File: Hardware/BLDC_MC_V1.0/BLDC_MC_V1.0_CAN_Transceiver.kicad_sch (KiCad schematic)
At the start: 15 parts, among them U2 TCAN334DR

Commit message: Update recovery files of the project
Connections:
- net IC_TXD: now reaches R11.1, U2.1 (TXD)
- net IC_RXD: now reaches R12.1, U2.4 (RXD)
- net SHDN: now reaches C15.1, R9.1, U2.5 (SHDN)
- net CANL: now reaches FL1.2, U2.6 (CANL)
- net CANH: now reaches FL1.1, U2.7 (CANH)
- net STB: now reaches C14.1, R10.1, U2.8 (STB)
- net Split_CAP: now reaches C16.1, R13.2, R14.1
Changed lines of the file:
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@@
+		)
+	)
+	(label "SHDN"
+		(at 110.49 83.82 0)
+		(effects
+			(font
+				(size 1.27 1.27)
+			)
+			(justify left bottom)
+		)
+	)
+	(label "CANH"
+		(at 157.48 83.82 0)
+		(effects
+			(font
+				(size 1.27 1.27)
+			)
+			(justify left bottom)
+		)
+	)
+	(label "IC_RXD"
+		(at 107.95 91.44 0)
+		(effects
+			(font
+				(size 1.27 1.27)
+			)
+			(justify left bottom)
+		)
+	)
+	(label "STB"
+		(at 110.49 86.36 0)
+		(effects
+			(font
+				(size 1.27 1.27)
+			)
+			(justify left bottom)
+		)
+	)
+	(label "CANL"
+		(at 157.48 91.44 0)
+		(effects
+			(font
+				(size 1.27 1.27)
+			)
+			(justify left bottom)
+		)
+	)
+	(label "IC_TXD"
+		(at 107.95 88.9 0)
+		(effects
+			(font
+				(size 1.27 1.27)
+			)
+			(justify left bottom)
+		)
+	)
+	(label "Split_CAP"
+		(at 203.2 87.63 0)
+		(effects
+			(font
+				(size 1.27 1.27)
+			)
+			(justify left bottom)
 		)
 	)

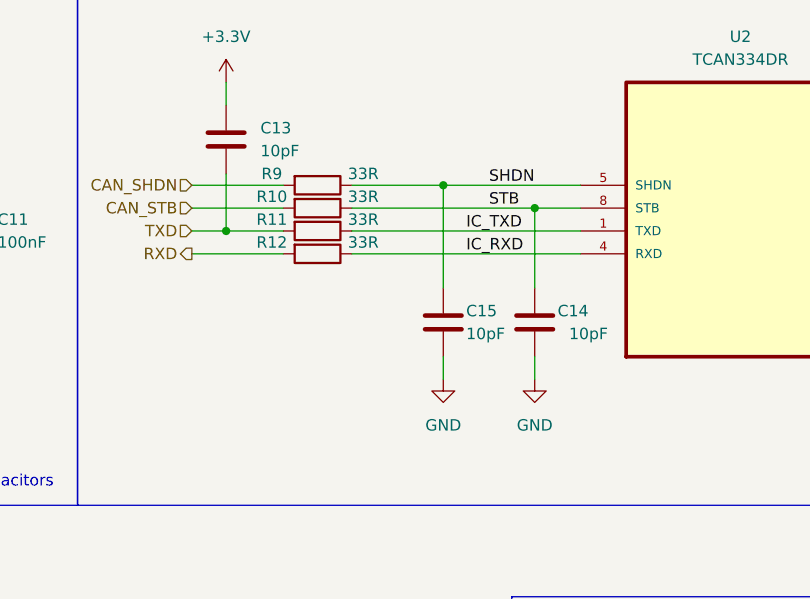
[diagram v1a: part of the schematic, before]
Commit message: Update the component placement of the board
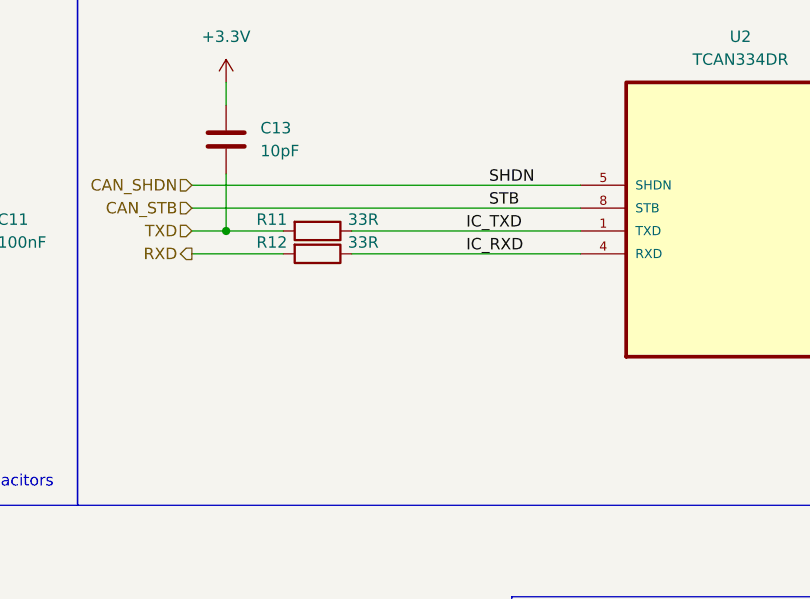
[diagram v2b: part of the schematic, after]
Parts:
- removed C14, C15: 10pF, Capacitor_SMD:C_0603_1608Metric, symbol Device:C
- removed R10, R9: 33R, Resistor_SMD:R_0603_1608Metric, symbol Device:R
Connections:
- net SHDN is gone; now on net CAN_SHDN: U2.5 (SHDN)
- net STB is gone; now on net CAN_STB: U2.8 (STB)

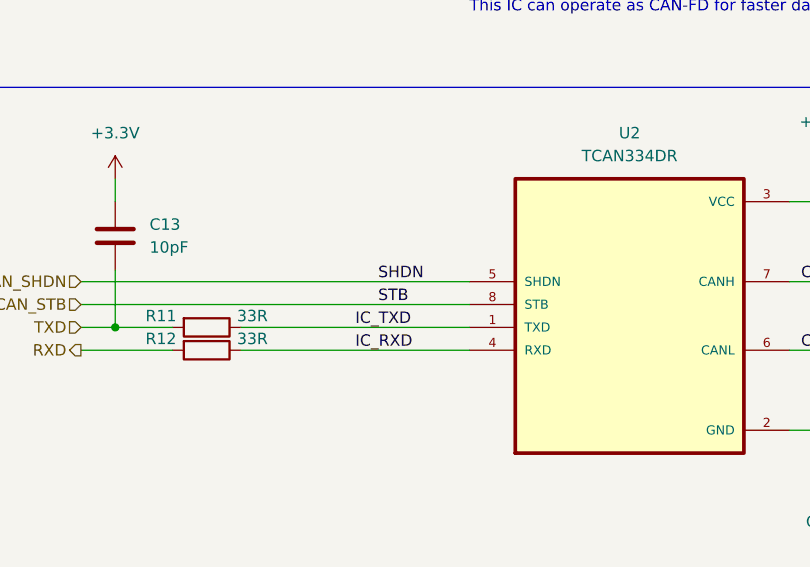
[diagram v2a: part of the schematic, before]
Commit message: Update the components' placement of the board
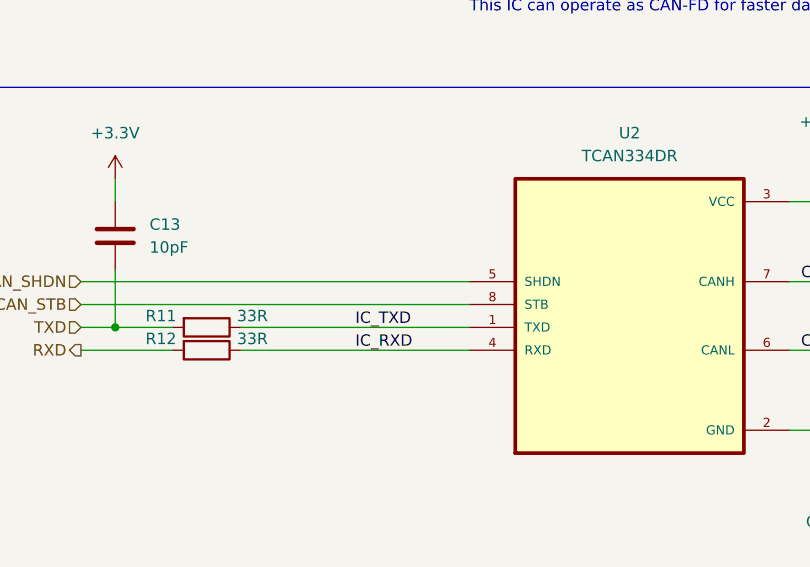
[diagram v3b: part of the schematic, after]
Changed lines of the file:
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@@
-		)
-	)
-	(label "SHDN"
-		(at 110.49 83.82 0)
-		(effects
-			(font
-				(size 1.27 1.27)
-			)
-			(justify left bottom)
 		)
 	)
@@
 		(effects
 			(font
-				(size 1.27 1.27)
-			)
-			(justify left bottom)
-		)
-	)
-	(label "STB"
-		(at 110.49 86.36 0)
-		(effects
-			(font
